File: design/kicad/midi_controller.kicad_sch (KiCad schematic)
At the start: 14 parts, among them J1 Conn_01x05

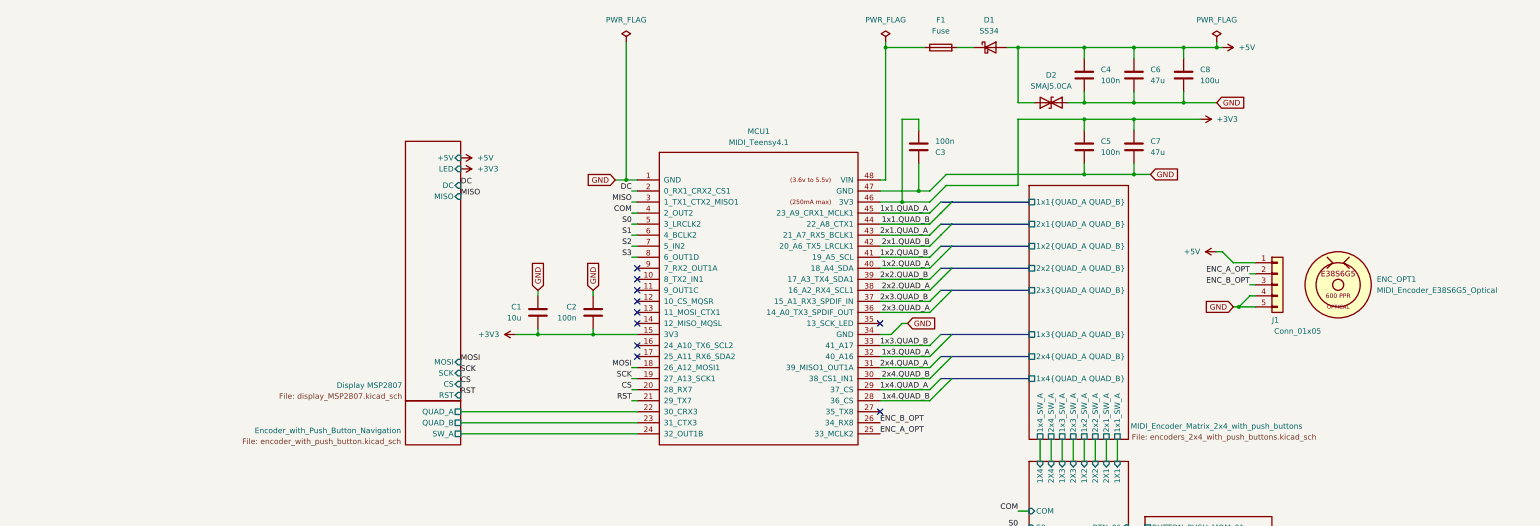
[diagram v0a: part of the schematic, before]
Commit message: Update capacitor references in multiplexer schematic
Changed capacitor references from C11 to C42 and C12 to C43 in the multiplexer_CD74HC4067M schematic. Updated instances accordingly to maintain consistency in the design.
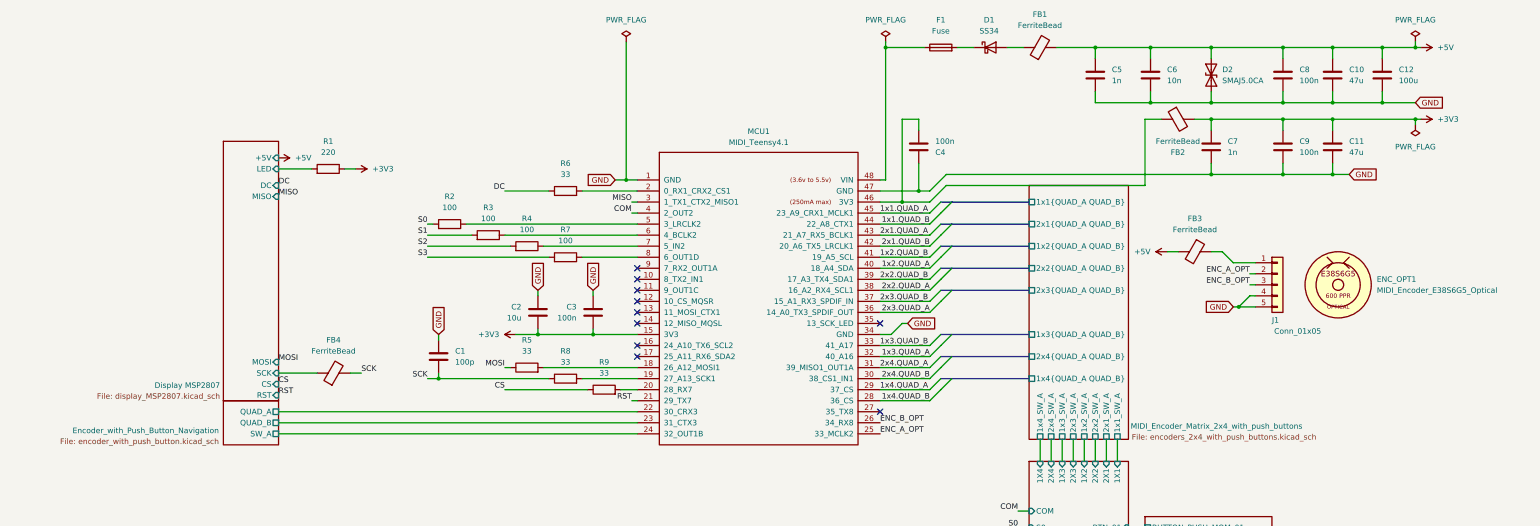
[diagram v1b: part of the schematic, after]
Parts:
- added C1: 100p, Capacitor_SMD:C_0603_1608Metric, symbol Device:C
- added C5, C7: 1n, Capacitor_SMD:C_0603_1608Metric, symbol Device:C
- added C6: 10n, Capacitor_SMD:C_0603_1608Metric, symbol Device:C
- added FB1, FB2, FB3, FB4: FerriteBead, Inductor_SMD:L_0805_2012Metric, symbol Device:FerriteBead
- added R1: 220, Resistor_SMD:R_0603_1608Metric, symbol Device:R
- added R2, R3, R4, R7: 100, Resistor_SMD:R_0603_1608Metric, symbol Device:R
- added R5, R6, R8, R9: 33, Resistor_SMD:R_0603_1608Metric, symbol Device:R
- renumbered C6 to C10, C7 to C11, C8 to C12, C1 to C2, C2 to C3, C3 to C4, C4 to C8, C5 to C9
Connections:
- net +3V3: now also C7.1, FB2.2, R1.1; no longer C4.1, MCU1.46 (3V3)
- net +5V: now also D2.2 (A2), C5.1, C6.1, FB1.2, FB3.2; no longer D1.2 (A), D2.1 (A1), J1.1 (Pin_1)
- net CS: now also R9.1; no longer MCU1.20 (28_RX7)
- net DC: now also R6.1; no longer MCU1.2 (0_RX1_CRX2_CS1)
- net GND: now also D2.1 (A1), C1.2, C5.2, C6.2, C7.2; no longer D2.2 (A2)
- net MOSI: now also R5.1; no longer MCU1.18 (26_A12_MOSI1)
- net S0: now also R2.2; no longer MCU1.5 (3_LRCLK2)
- net S1: now also R3.2; no longer MCU1.6 (4_BCLK2)
- net S2: now also R4.2; no longer MCU1.7 (5_IN2)
- net S3: now also R7.2; no longer MCU1.8 (6_OUT1D)
- net SCK: now also C1.1, FB4.2, R8.1; no longer MCU1.19 (27_A13_SCK1)
- new net: MCU1.19 (27_A13_SCK1), R8.2
- new net: MCU1.5 (3_LRCLK2), R2.1
- new net: D1.2 (A), FB1.1
- new net: MCU1.18 (26_A12_MOSI1), R5.2
- new net: MCU1.20 (28_RX7), R9.2
- new net: MCU1.2 (0_RX1_CRX2_CS1), R6.2
- new net: MCU1.7 (5_IN2), R4.1
- new net: C4.1, FB2.1, MCU1.46 (3V3)
- new net: MCU1.6 (4_BCLK2), R3.1
- new net: MCU1.8 (6_OUT1D), R7.1
- new net: FB3.1, J1.1 (Pin_1)
- new net Display MSP2807/LED: R1.2
- new net Display MSP2807/SCK: FB4.1
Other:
- moved on the sheet: C10, C11, C12, C8, C9, D2

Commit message: Update kicad binary files
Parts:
- renumbered FB4 to FB1, FB1 to FB2, FB2 to FB3, FB3 to FB4
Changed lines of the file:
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@@
 		(dnp no)
 		(fields_autoplaced yes)
-		(property "Reference" "FB1"
+		(property "Reference" "FB2"
 			(at 251.4092 67.31 90)
 			(effects
@@
 			(project ""
 				(path "/9e44e663-00d0-4f33-bf1f-c4ad78deb554"
-					(reference "FB1")
+					(reference "FB2")
 					(unit 1)
 				)
@@
 		(dnp no)
 		(fields_autoplaced yes)
-		(property "Reference" "FB4"
+		(property "Reference" "FB1"
 			(at 88.8492 142.24 90)
 			(effects
@@
 			(project "midi_controller"
 				(path "/9e44e663-00d0-4f33-bf1f-c4ad78deb554"
-					(reference "FB4")
+					(reference "FB1")
 					(unit 1)
 				)
@@
 		(dnp no)
 		(fields_autoplaced yes)
-		(property "Reference" "FB3"
+		(property "Reference" "FB4"
 			(at 287.0708 114.3 90)
 			(effects
@@
 			(project "midi_controller"
 				(path "/9e44e663-00d0-4f33-bf1f-c4ad78deb554"
-					(reference "FB3")
+					(reference "FB4")
 					(unit 1)
 				)
@@
 		(on_board yes)
 		(dnp no)
-		(property "Reference" "FB2"
+		(property "Reference" "FB3"
 			(at 283.1592 99.06 90)
 			(effects
@@
 			(project "midi_controller"
 				(path "/9e44e663-00d0-4f33-bf1f-c4ad78deb554"
-					(reference "FB2")
-					(unit 1)
-				)
+					(reference "FB3")
+					(unit 1)
+				)

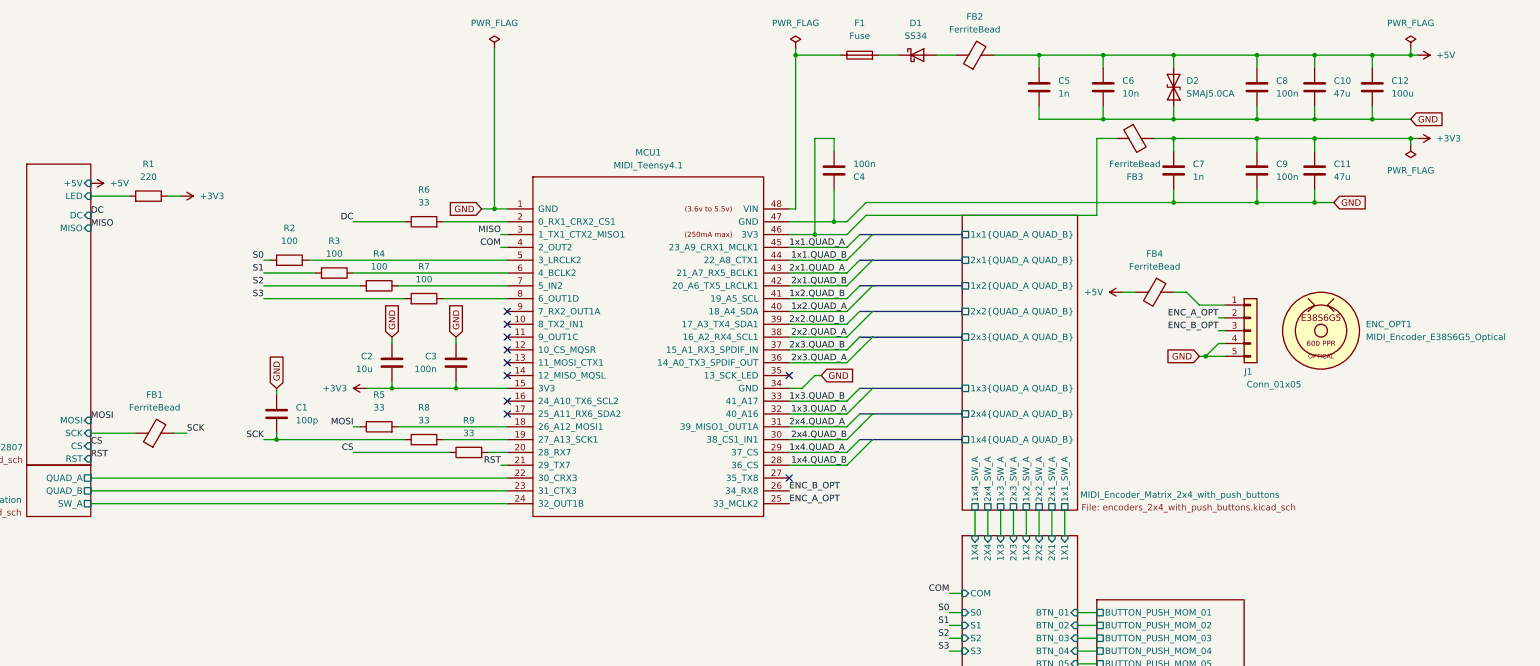
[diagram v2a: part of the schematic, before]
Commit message: Update kicad binary files
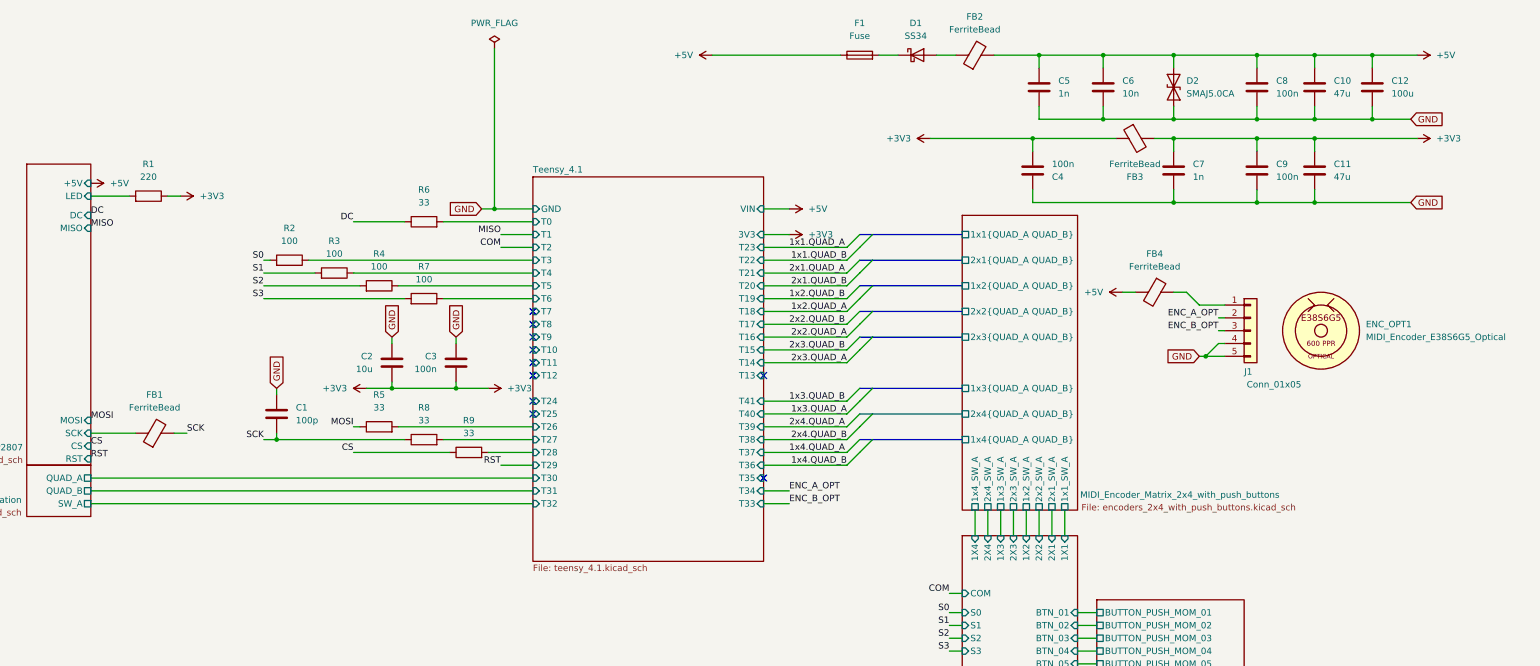
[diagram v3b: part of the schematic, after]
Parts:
- removed MCU1: MIDI_Teensy4.1, midi_controller:Teensy41, symbol midi_controller:MIDI_Teensy4.1
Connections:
- net +3V3: now also C4.1, FB3.1
- net +5V: now also F1.1
- net Teensy_4.1/T27: now reaches R8.2
- net Teensy_4.1/T3: now reaches R2.1
- net Teensy_4.1/T26: now reaches R5.2
- net Teensy_4.1/T28: now reaches R9.2
- net Teensy_4.1/T0: now reaches R6.2
- net Teensy_4.1/T5: now reaches R4.1
- net Teensy_4.1/T4: now reaches R3.1
- net Teensy_4.1/T6: now reaches R7.1
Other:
- added sheet Teensy_4.1 (teensy_4.1.kicad_sch)
- moved on the sheet: C4

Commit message: Update kicad binary files
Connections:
- net Display MSP2807/SCK is gone; now on net SCK: FB1.1
- net Teensy_4.1/T0 is gone; now on net DC: R6.2
- net Teensy_4.1/T3 is gone; now on net S0: R2.1
- net Teensy_4.1/T4 is gone; now on net S1: R3.1
- net Teensy_4.1/T5 is gone; now on net S2: R4.1
- net Teensy_4.1/T6 is gone; now on net S3: R7.1
- net SCK: no longer C1.1, FB1.2, R8.1
- net Display MSP2807/LED renamed LED
- new net: C1.1, FB1.2, R8.1
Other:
- moved on the sheet: C10, C11, C12, C2, C3, C4, C5, C6, C7, C8, C9, D1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

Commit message: Update kicad binary files
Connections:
- net ENC_A_OPT renamed OPT.QUAD_A
- net ENC_B_OPT renamed OPT.QUAD_B
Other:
- moved on the sheet: C10, C11, C12, C2, C3, C4, C5, C6, C7, C9, D2, FB3
